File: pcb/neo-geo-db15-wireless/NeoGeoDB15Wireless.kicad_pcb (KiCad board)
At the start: 2 copper layers, 39.9 x 32 mm, 3 parts, among them J1 DB15_Female_MountingHoles, U1 RP2040-Zero, U2 NRF24L01

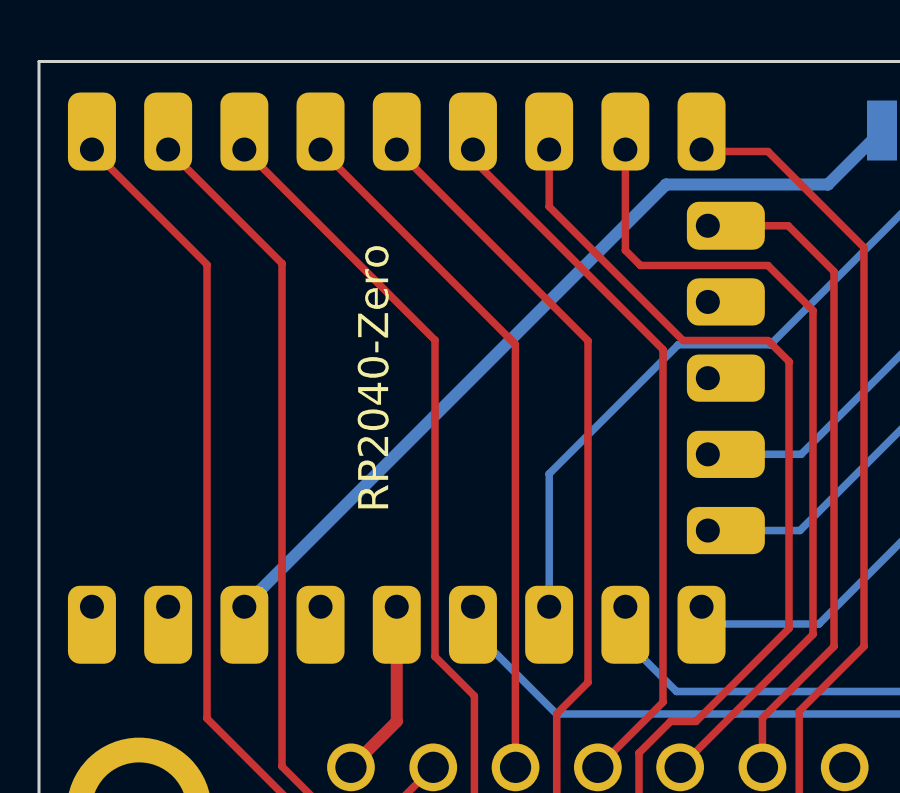
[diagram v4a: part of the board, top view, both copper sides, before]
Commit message: Adds decoupling caps
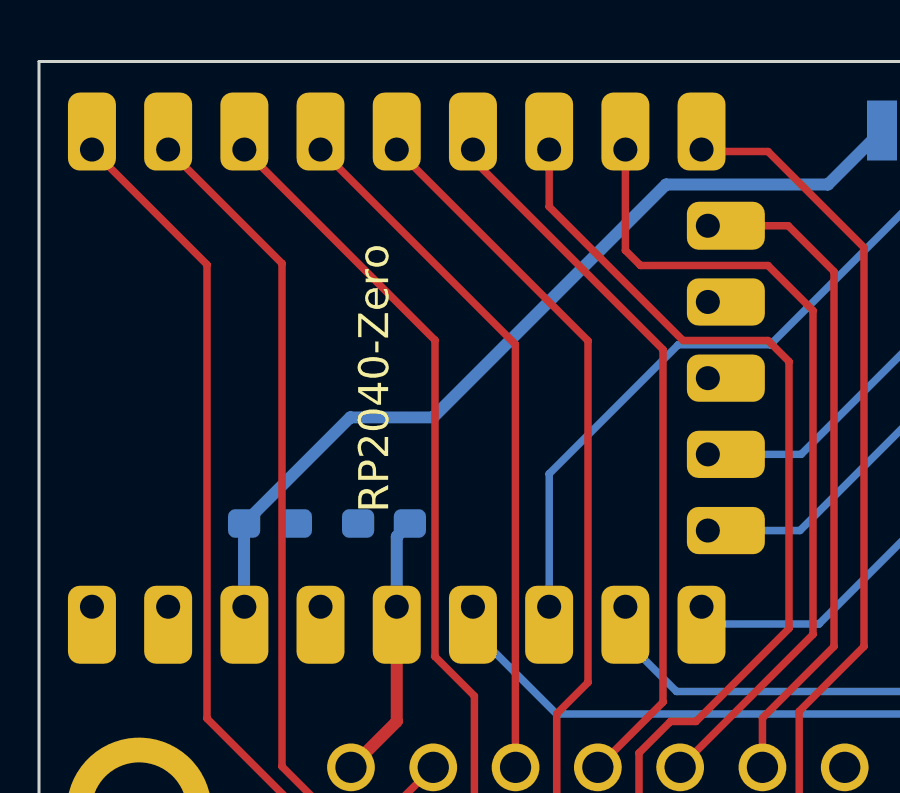
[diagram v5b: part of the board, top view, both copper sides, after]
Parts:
- added C1: 0.1uF, Capacitor_SMD:C_0603_1608Metric_Pad1.08x0.95mm_HandSolder, B.Cu at (91.5, 76.9)
- added C2: 0.1uF, Capacitor_SMD:C_0603_1608Metric_Pad1.08x0.95mm_HandSolder, B.Cu at (87.7, 76.9)
- U2: value NRF24L01 -> NRF24L01_Breakout
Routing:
- net /VCC: track 5.99 -> 8.94 mm
- net /3V3: track 27.8 -> 29.5 mm
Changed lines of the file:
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@@
       (effects (font (size 1 1) (thickness 0.15)) (justify mirror))
     )
-    (fp_text value "NRF24L01" (at 0 7.75 180 unlocked) (layer "B.SilkS")
+    (fp_text value "NRF24L01_Breakout" (at 0 7.75 180 unlocked) (layer "B.SilkS")
       (effects (font (size 1 1) (thickness 0.15)) (justify mirror))
     )
@@
     )
   )
+  (footprint "Capacitor_SMD:C_0603_1608Metric_Pad1.08x0.95mm_HandSolder" (layer "B.Cu")
+    (at 87.7 76.9)
+    (descr "Capacitor SMD 0603 (1608 Metric), square (rectangular) end terminal, IPC_7351 nominal with elongated pad for handsoldering. (Body size source: IPC-SM-782 page 76, https://www.pcb-3d.com/wordpress/wp-content/uploads/ipc-sm-782a_amendment_1_and_2.pdf), generated with kicad-footprint-generator")
+    (tags "capacitor handsolder")
+    (property "Sheetfile" "NeoGeoDB15Wireless.kicad_sch")
+    (property "Sheetname" "")
+    (attr smd)
+    (fp_text reference "C2" (at 0 -1.7) (layer "B.SilkS")
+      (effects (font (size 1 1) (thickness 0.15)) (justify mirror))
+    )
+    (fp_text value "0.1uF" (at 0 -1.43) (layer "B.Fab")
+      (effects (font (size 1 1) (thickness 0.15)) (justify mirror))
+    )
+    (fp_text user "${REFERENCE}" (at 0 0) (layer "B.Fab")
+      (effects (font (size 0.4 0.4) (thickness 0.06)) (justify mirror))
+    )
+    (fp_line (start -0.146267 -0.51) (end 0.146267 -0.51) (layer "B.SilkS") (width 0.12))
+    (fp_line (start -0.146267 0.51) (end 0.146267 0.51) (layer "B.SilkS") (width 0.12))
+    (fp_line (start -1.65 0.73) (end 1.65 0.73) (layer "B.CrtYd") (width 0.05))
+    (fp_line (start 1.65 0.73) (end 1.65 -0.73) (layer "B.CrtYd") (width 0.05))
+    (fp_line (start 1.65 -0.73) (end -1.65 -0.73) (layer "B.CrtYd") (width 0.05))
+    (fp_line (start -1.65 -0.73) (end -1.65 0.73) (layer "B.CrtYd") (width 0.05))
+    (fp_line (start 0.8 -0.4) (end -0.8 -0.4) (layer "B.Fab") (width 0.1))
+    (fp_line (start -0.8 -0.4) (end -0.8 0.4) (layer "B.Fab") (width 0.1))
+    (fp_line (start -0.8 0.4) (end 0.8 0.4) (layer "B.Fab") (width 0.1))
+    (fp_line (start 0.8 0.4) (end 0.8 -0.4) (layer "B.Fab") (width 0.1))
+    (pad "1" smd roundrect (at -0.8625 0) (size 1.075 0.95) (layers "B.Cu" "B.Paste" "B.Mask") (roundrect_rratio 0.25)
+      (net 24 "/3V3") (pintype "passive"))
+    (pad "2" smd roundrect (at 0.8625 0) (size 1.075 0.95) (layers "B.Cu" "B.Paste" "B.Mask") (roundrect_rratio 0.25)
+      (net 10 "/GND") (pintype "passive"))
+    (model "${KICAD6_3DMODEL_DIR}/Capacitor_SMD.3dshapes/C_0603_1608Metric.wrl"
+      (offset (xyz 0 0 0))
+      (scale (xyz 1 1 1))
+      (rotate (xyz 0 0 0))
+    )
+  )
+  (footprint "Capacitor_SMD:C_0603_1608Metric_Pad1.08x0.95mm_HandSolder" (layer "B.Cu")
+    (at 91.5 76.9 180)
+    (descr "Capacitor SMD 0603 (1608 Metric), square (rectangular) end terminal, IPC_7351 nominal with elongated pad for handsoldering. (Body size source: IPC-SM-782 page 76, https://www.pcb-3d.com/wordpress/wp-content/uploads/ipc-sm-782a_amendment_1_and_2.pdf), generated with kicad-footprint-generator")
+    (tags "capacitor handsolder")
+    (property "Sheetfile" "NeoGeoDB15Wireless.kicad_sch")
+    (property "Sheetname" "")
+    (attr smd)
+    (fp_text reference "C1" (at 0 1.7) (layer "B.SilkS")
+      (effects (font (size 1 1) (thickness 0.15)) (justify mirror))
+    )
+    (fp_text value "0.1uF" (at 0 -1.43) (layer "B.Fab")
+      (effects (font (size 1 1) (thickness 0.15)) (justify mirror))
+    )
+    (fp_text user "${REFERENCE}" (at 0 0) (layer "B.Fab")
+      (effects (font (size 0.4 0.4) (thickness 0.06)) (justify mirror))
+    )
+    (fp_line (start -0.146267 0.51) (end 0.146267 0.51) (layer "B.SilkS") (width 0.12))
+    (fp_line (start -0.146267 -0.51) (end 0.146267 -0.51) (layer "B.SilkS") (width 0.12))
+    (fp_line (start 1.65 -0.73) (end -1.65 -0.73) (layer "B.CrtYd") (width 0.05))
+    (fp_line (start 1.65 0.73) (end 1.65 -0.73) (layer "B.CrtYd") (width 0.05))
+    (fp_line (start -1.65 0.73) (end 1.65 0.73) (layer "B.CrtYd") (width 0.05))
+    (fp_line (start -1.65 -0.73) (end -1.65 0.73) (layer "B.CrtYd") (width 0.05))
+    (fp_line (start 0.8 0.4) (end 0.8 -0.4) (layer "B.Fab") (width 0.1))
+    (fp_line (start -0.8 0.4) (end 0.8 0.4) (layer "B.Fab") (width 0.1))
+    (fp_line (start -0.8 -0.4) (end -0.8 0.4) (layer "B.Fab") (width 0.1))
+    (fp_line (start 0.8 -0.4) (end -0.8 -0.4) (layer "B.Fab") (width 0.1))
+    (pad "1" smd roundrect (at -0.8625 0 180) (size 1.075 0.95) (layers "B.Cu" "B.Paste" "B.Mask") (roundrect_rratio 0.25)
+      (net 3 "/VCC") (pintype "passive"))
+    (pad "2" smd roundrect (at 0.8625 0 180) (size 1.075 0.95) (layers "B.Cu" "B.Paste" "B.Mask") (roundrect_rratio 0.25)
+      (net 10 "/GND") (pintype "passive"))
+    (model "${KICAD6_3DMODEL_DIR}/Capacitor_SMD.3dshapes/C_0603_1608Metric.wrl"
+      (offset (xyz 0 0 0))
+      (scale (xyz 1 1 1))
+      (rotate (xyz 0 0 0))
+    )
+  )
   (gr_rect (start 118.5 62.25) (end 106.5 81.75) (layer "B.SilkS") (width 0.15) (fill none))
   (gr_rect (start 80 93.5) (end 119.9 61.5) (layer "Edge.Cuts") (width 0.1) (fill none))
@@
   (segment (start 90.398799 85.0284) (end 91.925 83.502199) (width 0.4) (layer "F.Cu") (net 3))
   (segment (start 91.925 83.502199) (end 91.925 79.675) (width 0.4) (layer "F.Cu") (net 3))
+  (segment (start 91.925 79.675) (end 91.925 77.3375) (width 0.4) (layer "B.Cu") (net 3))
+  (segment (start 91.925 77.3375) (end 92.3625 76.9) (width 0.4) (layer "B.Cu") (net 3))
   (segment (start 88.1 68.23) (end 84.305 64.435) (width 0.25) (layer "F.Cu") (net 4))
   (segment (start 93.141998 85.0284) (end 91.770398 86.4) (width 0.25) (layer "F.Cu") (net 4))
@@
   (segment (start 97.25 83.25) (end 94.465 80.465) (width 0.25) (layer "B.Cu") (net 21))
   (segment (start 111.25 83.25) (end 97.25 83.25) (width 0.25) (layer "B.Cu") (net 21))
+  (segment (start 90.375 73.3625) (end 93.1375 73.3625) (width 0.4) (layer "B.Cu") (net 24))
   (segment (start 106.3 65.6) (end 108.1 63.8) (width 0.4) (layer "B.Cu") (net 24))
-  (segment (start 86.845 79.655) (end 100.9 65.6) (width 0.4) (layer "B.Cu") (net 24))
-  (segment (start 86.845 79.675) (end 86.845 79.655) (width 0.4) (layer "B.Cu") (net 24))
+  (segment (start 86.8375 79.6675) (end 86.8375 76.9) (width 0.4) (layer "B.Cu") (net 24))
   (segment (start 100.9 65.6) (end 106.3 65.6) (width 0.4) (layer "B.Cu") (net 24))
+  (segment (start 86.8375 76.9) (end 90.375 73.3625) (width 0.4) (layer "B.Cu") (net 24))
+  (segment (start 93.1375 73.3625) (end 100.9 65.6) (width 0.4) (layer "B.Cu") (net 24))
   (zone (net 10) (net_name "/GND") (layers F&B.Cu) (hatch edge 0.508)
     (connect_pads (clearance 0.508))

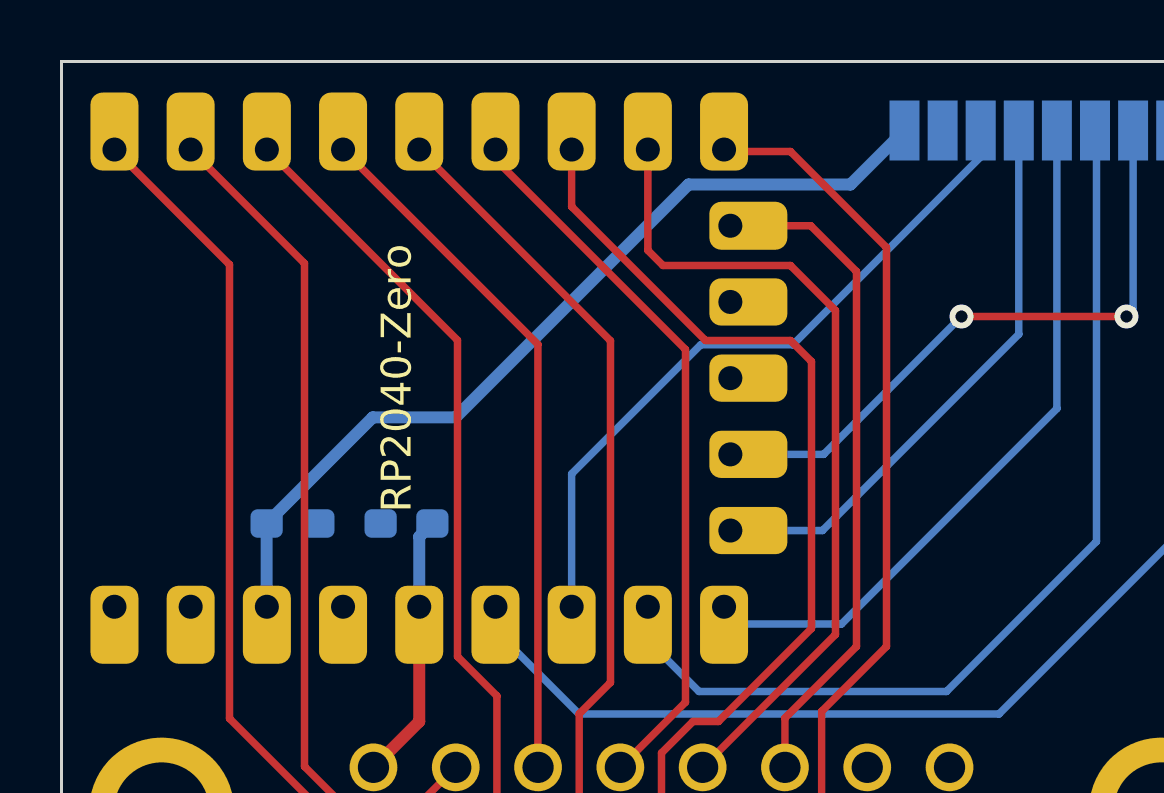
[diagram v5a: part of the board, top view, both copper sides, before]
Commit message: Increases ground plane
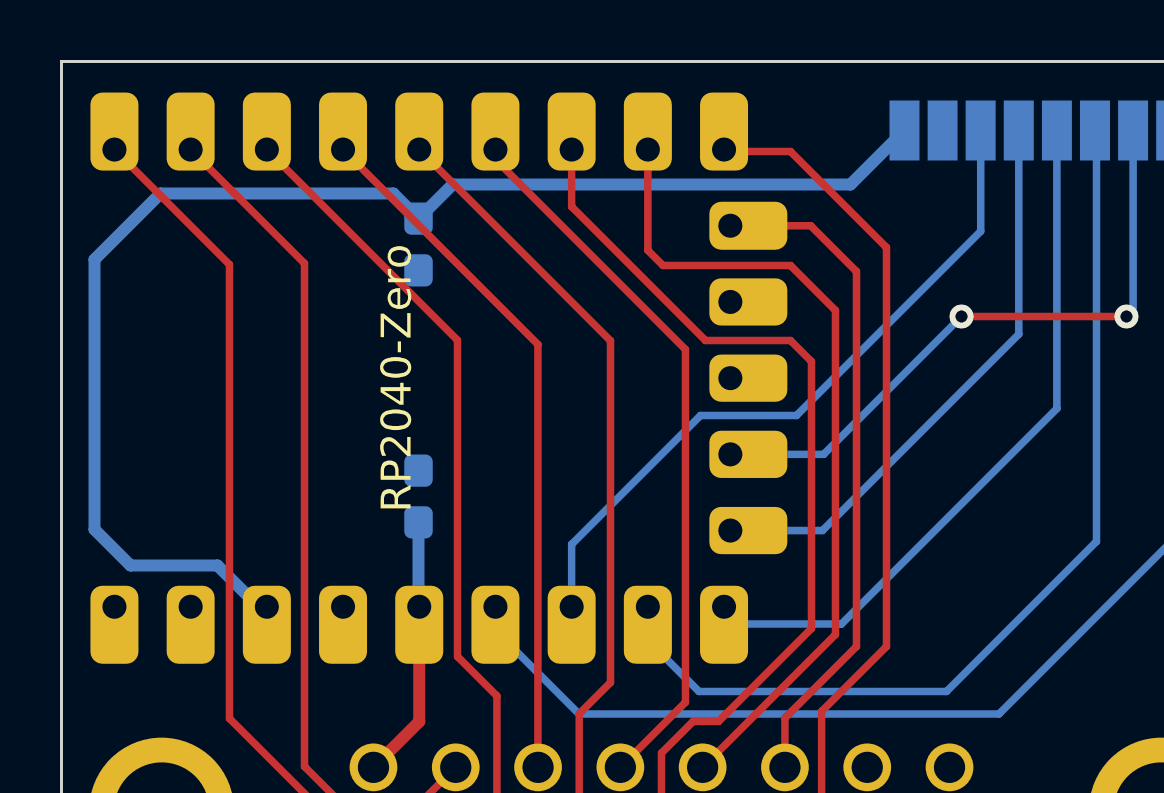
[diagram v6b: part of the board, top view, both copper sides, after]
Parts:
- U2: value NRF24L01_Breakout -> NRF24L01
- moved C2 10.2 mm to (91.9, 67.6), turned to -90 degrees
- moved C1 0.98 mm to (91.9, 76.0), turned to 90 degrees
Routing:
- net /3V3: track 29.5 -> 45.3 mm
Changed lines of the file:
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@@
       (effects (font (size 1 1) (thickness 0.15)) (justify mirror))
     )
-    (fp_text value "NRF24L01_Breakout" (at 0 7.75 180 unlocked) (layer "B.SilkS")
+    (fp_text value "NRF24L01" (at 0 7.75 180 unlocked) (layer "B.SilkS")
       (effects (font (size 1 1) (thickness 0.15)) (justify mirror))
     )
@@
   )
   (footprint "Capacitor_SMD:C_0603_1608Metric_Pad1.08x0.95mm_HandSolder" (layer "B.Cu")
-    (at 87.7 76.9)
+    (at 91.9 67.6 -90)
     (descr "Capacitor SMD 0603 (1608 Metric), square (rectangular) end terminal, IPC_7351 nominal with elongated pad for handsoldering. (Body size source: IPC-SM-782 page 76, https://www.pcb-3d.com/wordpress/wp-content/uploads/ipc-sm-782a_amendment_1_and_2.pdf), generated with kicad-footprint-generator")
     (tags "capacitor handsolder")
@@
     (property "Sheetname" "")
     (attr smd)
-    (fp_text reference "C2" (at 0 -1.7) (layer "B.SilkS")
-      (effects (font (size 1 1) (thickness 0.15)) (justify mirror))
-    )
-    (fp_text value "0.1uF" (at 0 -1.43) (layer "B.Fab")
-      (effects (font (size 1 1) (thickness 0.15)) (justify mirror))
-    )
-    (fp_text user "${REFERENCE}" (at 0 0) (layer "B.Fab")
+    (fp_text reference "C2" (at 0 -1.7 90) (layer "B.SilkS")
+      (effects (font (size 1 1) (thickness 0.15)) (justify mirror))
+    )
+    (fp_text value "0.1uF" (at 0 -1.43 90) (layer "B.Fab")
+      (effects (font (size 1 1) (thickness 0.15)) (justify mirror))
+    )
+    (fp_text user "${REFERENCE}" (at 0 0 90) (layer "B.Fab")
       (effects (font (size 0.4 0.4) (thickness 0.06)) (justify mirror))
     )
@@
     (fp_line (start -0.8 0.4) (end 0.8 0.4) (layer "B.Fab") (width 0.1))
     (fp_line (start 0.8 0.4) (end 0.8 -0.4) (layer "B.Fab") (width 0.1))
-    (pad "1" smd roundrect (at -0.8625 0) (size 1.075 0.95) (layers "B.Cu" "B.Paste" "B.Mask") (roundrect_rratio 0.25)
+    (pad "1" smd roundrect (at -0.8625 0 270) (size 1.075 0.95) (layers "B.Cu" "B.Paste" "B.Mask") (roundrect_rratio 0.25)
       (net 24 "/3V3") (pintype "passive"))
-    (pad "2" smd roundrect (at 0.8625 0) (size 1.075 0.95) (layers "B.Cu" "B.Paste" "B.Mask") (roundrect_rratio 0.25)
+    (pad "2" smd roundrect (at 0.8625 0 270) (size 1.075 0.95) (layers "B.Cu" "B.Paste" "B.Mask") (roundrect_rratio 0.25)
       (net 10 "/GND") (pintype "passive"))
     (model "${KICAD6_3DMODEL_DIR}/Capacitor_SMD.3dshapes/C_0603_1608Metric.wrl"
@@
   )
   (footprint "Capacitor_SMD:C_0603_1608Metric_Pad1.08x0.95mm_HandSolder" (layer "B.Cu")
-    (at 91.5 76.9 180)
+    (at 91.9 76 90)
     (descr "Capacitor SMD 0603 (1608 Metric), square (rectangular) end terminal, IPC_7351 nominal with elongated pad for handsoldering. (Body size source: IPC-SM-782 page 76, https://www.pcb-3d.com/wordpress/wp-content/uploads/ipc-sm-782a_amendment_1_and_2.pdf), generated with kicad-footprint-generator")
     (tags "capacitor handsolder")
@@
     (property "Sheetname" "")
     (attr smd)
-    (fp_text reference "C1" (at 0 1.7) (layer "B.SilkS")
-      (effects (font (size 1 1) (thickness 0.15)) (justify mirror))
-    )
-    (fp_text value "0.1uF" (at 0 -1.43) (layer "B.Fab")
-      (effects (font (size 1 1) (thickness 0.15)) (justify mirror))
-    )
-    (fp_text user "${REFERENCE}" (at 0 0) (layer "B.Fab")
+    (fp_text reference "C1" (at 0 1.7 90) (layer "B.SilkS")
+      (effects (font (size 1 1) (thickness 0.15)) (justify mirror))
+    )
+    (fp_text value "0.1uF" (at 0 -1.43 90) (layer "B.Fab")
+      (effects (font (size 1 1) (thickness 0.15)) (justify mirror))
+    )
+    (fp_text user "${REFERENCE}" (at 0 0 90) (layer "B.Fab")
       (effects (font (size 0.4 0.4) (thickness 0.06)) (justify mirror))
     )
@@
     (fp_line (start -0.8 -0.4) (end -0.8 0.4) (layer "B.Fab") (width 0.1))
     (fp_line (start 0.8 -0.4) (end -0.8 -0.4) (layer "B.Fab") (width 0.1))
-    (pad "1" smd roundrect (at -0.8625 0 180) (size 1.075 0.95) (layers "B.Cu" "B.Paste" "B.Mask") (roundrect_rratio 0.25)
+    (pad "1" smd roundrect (at -0.8625 0 90) (size 1.075 0.95) (layers "B.Cu" "B.Paste" "B.Mask") (roundrect_rratio 0.25)
       (net 3 "/VCC") (pintype "passive"))
-    (pad "2" smd roundrect (at 0.8625 0 180) (size 1.075 0.95) (layers "B.Cu" "B.Paste" "B.Mask") (roundrect_rratio 0.25)
+    (pad "2" smd roundrect (at 0.8625 0 90) (size 1.075 0.95) (layers "B.Cu" "B.Paste" "B.Mask") (roundrect_rratio 0.25)
       (net 10 "/GND") (pintype "passive"))
     (model "${KICAD6_3DMODEL_DIR}/Capacitor_SMD.3dshapes/C_0603_1608Metric.wrl"
@@
   (segment (start 90.398799 85.0284) (end 91.925 83.502199) (width 0.4) (layer "F.Cu") (net 3))
   (segment (start 91.925 83.502199) (end 91.925 79.675) (width 0.4) (layer "F.Cu") (net 3))
-  (segment (start 91.925 79.675) (end 91.925 77.3375) (width 0.4) (layer "B.Cu") (net 3))
-  (segment (start 91.925 77.3375) (end 92.3625 76.9) (width 0.4) (layer "B.Cu") (net 3))
+  (segment (start 91.9 76.8625) (end 91.9 79.65) (width 0.4) (layer "B.Cu") (net 3))
+  (segment (start 91.9 79.65) (end 91.925 79.675) (width 0.4) (layer "B.Cu") (net 3))
   (segment (start 88.1 68.23) (end 84.305 64.435) (width 0.25) (layer "F.Cu") (net 4))
   (segment (start 93.141998 85.0284) (end 91.770398 86.4) (width 0.25) (layer "F.Cu") (net 4))
@@
   (segment (start 114.5 63.85) (end 114.5 77.5) (width 0.25) (layer "B.Cu") (net 19))
   (segment (start 114.45 63.8) (end 114.5 63.85) (width 0.25) (layer "B.Cu") (net 19))
-  (segment (start 104.3774 70.9426) (end 101.3074 70.9426) (width 0.25) (layer "B.Cu") (net 20))
-  (segment (start 110.64 64.68) (end 104.3774 70.9426) (width 0.25) (layer "B.Cu") (net 20))
-  (segment (start 110.64 63.8) (end 110.64 64.68) (width 0.25) (layer "B.Cu") (net 20))
-  (segment (start 101.3074 70.9426) (end 97.005 75.245) (width 0.25) (layer "B.Cu") (net 20))
-  (segment (start 97.005 75.245) (end 97.005 79.675) (width 0.25) (layer "B.Cu") (net 20))
+  (segment (start 110.64 67.16) (end 104.5 73.3) (width 0.25) (layer "B.Cu") (net 20))
+  (segment (start 101.3 73.3) (end 97.005 77.595) (width 0.25) (layer "B.Cu") (net 20))
+  (segment (start 97.005 77.595) (end 97.005 79.675) (width 0.25) (layer "B.Cu") (net 20))
+  (segment (start 110.64 63.8) (end 110.64 67.16) (width 0.25) (layer "B.Cu") (net 20))
+  (segment (start 104.5 73.3) (end 101.3 73.3) (width 0.25) (layer "B.Cu") (net 20))
   (segment (start 116.99 63.8) (end 116.99 77.51) (width 0.25) (layer "B.Cu") (net 21))
   (segment (start 116.99 77.51) (end 111.25 83.25) (width 0.25) (layer "B.Cu") (net 21))
@@
   (segment (start 97.25 83.25) (end 94.465 80.465) (width 0.25) (layer "B.Cu") (net 21))
   (segment (start 111.25 83.25) (end 97.25 83.25) (width 0.25) (layer "B.Cu") (net 21))
-  (segment (start 90.375 73.3625) (end 93.1375 73.3625) (width 0.4) (layer "B.Cu") (net 24))
-  (segment (start 106.3 65.6) (end 108.1 63.8) (width 0.4) (layer "B.Cu") (net 24))
-  (segment (start 86.8375 79.6675) (end 86.8375 76.9) (width 0.4) (layer "B.Cu") (net 24))
-  (segment (start 100.9 65.6) (end 106.3 65.6) (width 0.4) (layer "B.Cu") (net 24))
-  (segment (start 86.8375 76.9) (end 90.375 73.3625) (width 0.4) (layer "B.Cu") (net 24))
-  (segment (start 93.1375 73.3625) (end 100.9 65.6) (width 0.4) (layer "B.Cu") (net 24))
+  (segment (start 81.1 68.1) (end 81.1 77.1) (width 0.4) (layer "B.Cu") (net 24))
+  (segment (start 106.3 65.6) (end 93.0375 65.6) (width 0.4) (layer "B.Cu") (net 24))
+  (segment (start 83.3 65.9) (end 81.1 68.1) (width 0.4) (layer "B.Cu") (net 24))
+  (segment (start 91.9 66.7375) (end 91.0625 65.9) (width 0.4) (layer "B.Cu") (net 24))
+  (segment (start 82.3 78.3) (end 85.2 78.3) (width 0.4) (layer "B.Cu") (net 24))
+  (segment (start 86.575 79.675) (end 86.845 79.675) (width 0.4) (layer "B.Cu") (net 24))
+  (segment (start 85.2 78.3) (end 86.575 79.675) (width 0.4) (layer "B.Cu") (net 24))
+  (segment (start 91.0625 65.9) (end 83.3 65.9) (width 0.4) (layer "B.Cu") (net 24))
+  (segment (start 108.1 63.8) (end 106.3 65.6) (width 0.4) (layer "B.Cu") (net 24))
+  (segment (start 81.1 77.1) (end 82.3 78.3) (width 0.4) (layer "B.Cu") (net 24))
+  (segment (start 93.0375 65.6) (end 91.9 66.7375) (width 0.4) (layer "B.Cu") (net 24))
   (zone (net 10) (net_name "/GND") (layers F&B.Cu) (hatch edge 0.508)
     (connect_pads (clearance 0.508))
